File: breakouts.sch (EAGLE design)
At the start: 7 parts

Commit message: Added USB C breakout with CC pulldown resistors
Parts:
- added CONN2: USB-C_WURTH_632723X00011USB-C, USB-C:USB-C_WURTH_632723X00011USB-C
- added JP1: (no value), SparkFun:M06SIP
- added R2, R3: 5K1, SparkFun-Passives:RESISTOR0603-RES
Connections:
- removed net N$10: U$2.NC
- new net CC1_SA: CONN2.CC1, JP1.2, R3.2
- new net CC2_SA: CONN2.CC2, JP1.3, R2.2
- new net DN_SA: CONN2.DN1, CONN2.DN2, JP1.5
- new net DP_SA: CONN2.DP1, CONN2.DP2, JP1.4
- new net VBUS_SA: CONN2.VBUS1, CONN2.VBUS2, CONN2.VBUS3, CONN2.VBUS4, JP1.1
- net GND: now also CONN1.SHIELD5, CONN1.SHIELD6, CONN1.SHIELD7, CONN1.SHIELD8, CONN2.GND0, CONN2.GND1, CONN2.GND3, CONN2.GND4, CONN2.SHIELD1, CONN2.SHIELD2, CONN2.SHIELD3, CONN2.SHIELD4, CONN2.SHIELD5, CONN2.SHIELD6, CONN2.SHIELD7, CONN2.SHIELD8, JP1.6, R2.1, R3.1
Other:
- note added: "USBC breakout"
- note added: "optional pulldown resistors for UFP operation"

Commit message: Added RJ12 breakout
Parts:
- added J1: RJ11, SparkFun-Connectors:RJ11-6PTH
- added JP2: (no value), SparkFun:M06SIP
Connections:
- new net N$1: J1.1, JP2.1
- new net N$2: J1.2, JP2.2
- new net N$3: J1.3, JP2.3
- new net N$4: J1.4, JP2.4
- new net N$5: J1.5, JP2.5
- new net N$6: J1.6, JP2.6
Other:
- note added: "RJ12 breakout"
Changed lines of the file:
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@@
 <layer number="54" name="bGND_GNDA" color="1" fill="9" visible="yes" active="no"/>
 <layer number="56" name="wert" color="7" fill="1" visible="yes" active="no"/>
+<layer number="57" name="tCAD" color="7" fill="1" visible="no" active="no"/>
+<layer number="90" name="Modules" color="5" fill="1" visible="yes" active="yes"/>
 <layer number="91" name="Nets" color="2" fill="1" visible="yes" active="yes"/>
 <layer number="92" name="Busses" color="1" fill="1" visible="yes" active="yes"/>
@@
 <layer number="97" name="Info" color="7" fill="1" visible="yes" active="yes"/>
 <layer number="98" name="Guide" color="6" fill="1" visible="yes" active="yes"/>
+<layer number="99" name="SpiceOrder" color="7" fill="1" visible="yes" active="yes"/>
 <layer number="100" name="Muster" color="7" fill="1" visible="no" active="no"/>
 <layer number="101" name="Patch_Top" color="12" fill="4" visible="yes" active="yes"/>
@@
 <layer number="108" name="tplace-old" color="10" fill="1" visible="yes" active="yes"/>
 <layer number="109" name="ref-old" color="11" fill="1" visible="yes" active="yes"/>
+<layer number="110" name="fp0" color="7" fill="1" visible="yes" active="yes"/>
+<layer number="111" name="LPC17xx" color="7" fill="1" visible="yes" active="yes"/>
+<layer number="112" name="tSilk" color="7" fill="1" visible="yes" active="yes"/>
+<layer number="113" name="IDFDebug" color="4" fill="1" visible="yes" active="yes"/>
 <layer number="116" name="Patch_BOT" color="9" fill="4" visible="yes" active="yes"/>
 <layer number="121" name="_tsilk" color="7" fill="1" visible="yes" active="yes"/>
 <layer number="122" name="_bsilk" color="7" fill="1" visible="yes" active="yes"/>
+<layer number="123" name="tTestmark" color="7" fill="1" visible="yes" active="yes"/>
+<layer number="124" name="bTestmark" color="7" fill="1" visible="yes" active="yes"/>
 <layer number="125" name="_tNames" color="7" fill="1" visible="yes" active="yes"/>
+<layer number="126" name="_bNames" color="7" fill="1" visible="yes" active="yes"/>
+<layer number="127" name="_tValues" color="7" fill="1" visible="yes" active="yes"/>
+<layer number="128" name="_bValues" color="7" fill="1" visible="yes" active="yes"/>
+<layer number="131" name="tAdjust" color="7" fill="1" visible="yes" active="yes"/>
+<layer number="132" name="bAdjust" color="7" fill="1" visible="yes" active="yes"/>
 <layer number="144" name="Drill_legend" color="7" fill="1" visible="yes" active="yes"/>
+<layer number="150" name="Notes" color="7" fill="1" visible="yes" active="yes"/>
 <layer number="151" name="HeatSink" color="7" fill="1" visible="yes" active="yes"/>
+<layer number="152" name="_bDocu" color="7" fill="1" visible="yes" active="yes"/>
+<layer number="153" name="FabDoc1" color="7" fill="1" visible="yes" active="yes"/>
+<layer number="154" name="FabDoc2" color="7" fill="1" visible="yes" active="yes"/>
+<layer number="155" name="FabDoc3" color="7" fill="1" visible="yes" active="yes"/>
 <layer number="199" name="Contour" color="7" fill="1" visible="yes" active="yes"/>
 <layer number="200" name="200bmp" color="1" fill="10" visible="yes" active="yes"/>
@@
 <layer number="223" name="223bmp" color="24" fill="1" visible="no" active="no"/>
 <layer number="224" name="224bmp" color="25" fill="1" visible="no" active="no"/>
+<layer number="248" name="Housing" color="7" fill="1" visible="yes" active="yes"/>
+<layer number="249" name="Edge" color="7" fill="1" visible="yes" active="yes"/>
 <layer number="250" name="Descript" color="3" fill="1" visible="no" active="no"/>
 <layer number="251" name="SMDround" color="12" fill="11" visible="no" active="no"/>
@@
 <part name="R3" library="SparkFun-Passives" deviceset="RESISTOR" device="0603-RES" value="5K1"/>
 <part name="JP1" library="SparkFun" deviceset="M06" device="SIP"/>
+<part name="J1" library="SparkFun-Connectors" deviceset="RJ11-6" device="PTH" value="RJ11"/>
+<part name="JP2" library="SparkFun" deviceset="M06" device="SIP"/>
 </parts>
 <sheets>
@@
 <wire x1="-266.7" y1="-78.74" x2="-266.7" y2="129.54" width="1.6764" layer="97"/>
 <text x="-175.26" y="17.78" size="6.4516" layer="97">USBC breakout</text>
+<text x="-220.98" y="-121.92" size="6.4516" layer="97">RJ12 breakout</text>
+<wire x1="-157.48" y1="-152.4" x2="-228.6" y2="-152.4" width="1.6764" layer="97"/>
+<wire x1="-157.48" y1="-152.4" x2="-157.48" y2="-101.6" width="1.6764" layer="97"/>
+<wire x1="-157.48" y1="-101.6" x2="-228.6" y2="-101.6" width="1.6764" layer="97"/>
+<wire x1="-228.6" y1="-101.6" x2="-228.6" y2="-152.4" width="1.6764" layer="97"/>
 </plain>
 <instances>
@@
 <instance part="R3" gate="G$1" x="-149.86" y="71.12" rot="R90"/>
 <instance part="JP1" gate="G$1" x="-114.3" y="71.12" rot="R180"/>
+<instance part="J1" gate="G$1" x="-210.82" y="-137.16"/>
+<instance part="JP2" gate="G$1" x="-187.96" y="-137.16"/>
 </instances>
 <busses>
@@
 </segment>
 </net>
+<net name="N$1" class="0">
+<segment>
+<pinref part="J1" gate="G$1" pin="1"/>
+<pinref part="JP2" gate="G$1" pin="1"/>
+<wire x1="-205.74" y1="-142.24" x2="-182.88" y2="-142.24" width="0.1524" layer="91"/>
+</segment>
+</net>
+<net name="N$2" class="0">
+<segment>
+<pinref part="JP2" gate="G$1" pin="2"/>
+<pinref part="J1" gate="G$1" pin="2"/>
+<wire x1="-182.88" y1="-139.7" x2="-205.74" y2="-139.7" width="0.1524" layer="91"/>
+</segment>
+</net>
+<net name="N$3" class="0">
+<segment>
+<pinref part="J1" gate="G$1" pin="3"/>
+<pinref part="JP2" gate="G$1" pin="3"/>
+<wire x1="-205.74" y1="-137.16" x2="-182.88" y2="-137.16" width="0.1524" layer="91"/>
+</segment>
+</net>
+<net name="N$4" class="0">
+<segment>
+<pinref part="JP2" gate="G$1" pin="4"/>
+<pinref part="J1" gate="G$1" pin="4"/>
+<wire x1="-182.88" y1="-134.62" x2="-205.74" y2="-134.62" width="0.1524" layer="91"/>
+</segment>
+</net>
+<net name="N$5" class="0">
+<segment>
+<pinref part="J1" gate="G$1" pin="5"/>
+<pinref part="JP2" gate="G$1" pin="5"/>
+<wire x1="-205.74" y1="-132.08" x2="-182.88" y2="-132.08" width="0.1524" layer="91"/>
+</segment>
+</net>
+<net name="N$6" class="0">
+<segment>
+<pinref part="JP2" gate="G$1" pin="6"/>
+<pinref part="J1" gate="G$1" pin="6"/>
+<wire x1="-182.88" y1="-129.54" x2="-205.74" y2="-129.54" width="0.1524" layer="91"/>
+</segment>
+</net>

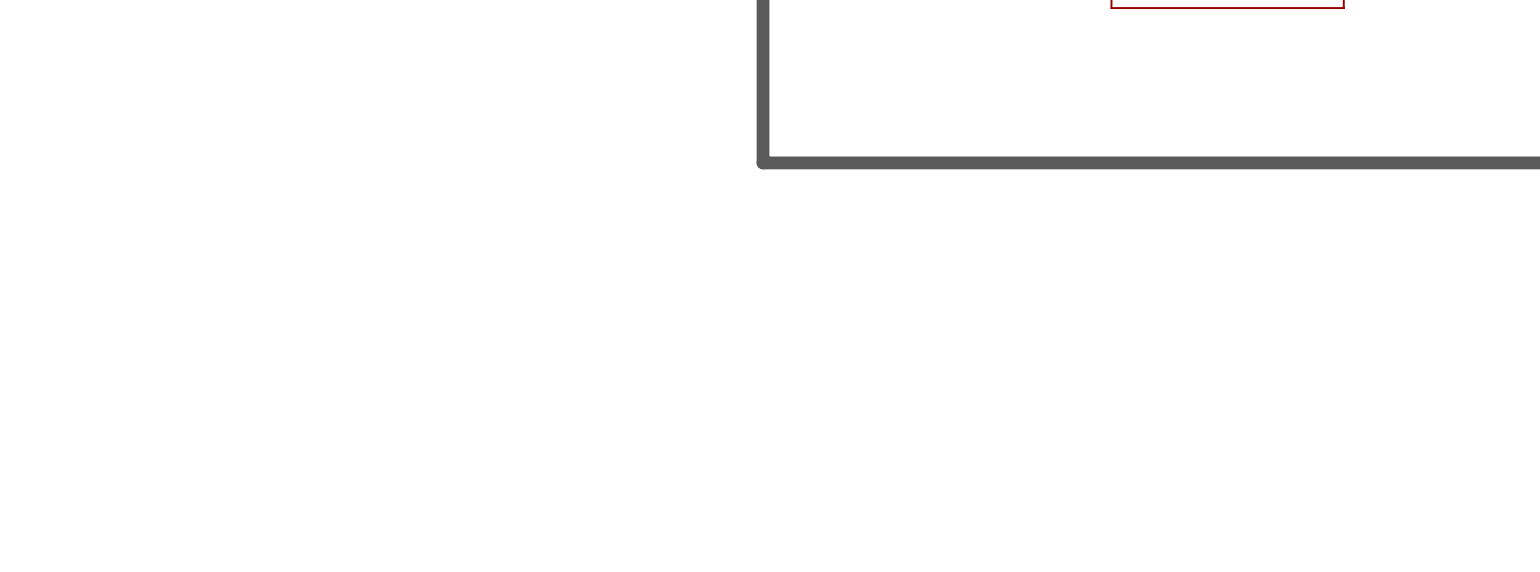
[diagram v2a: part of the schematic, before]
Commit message: Panalised breakouts and added powerpole breakout
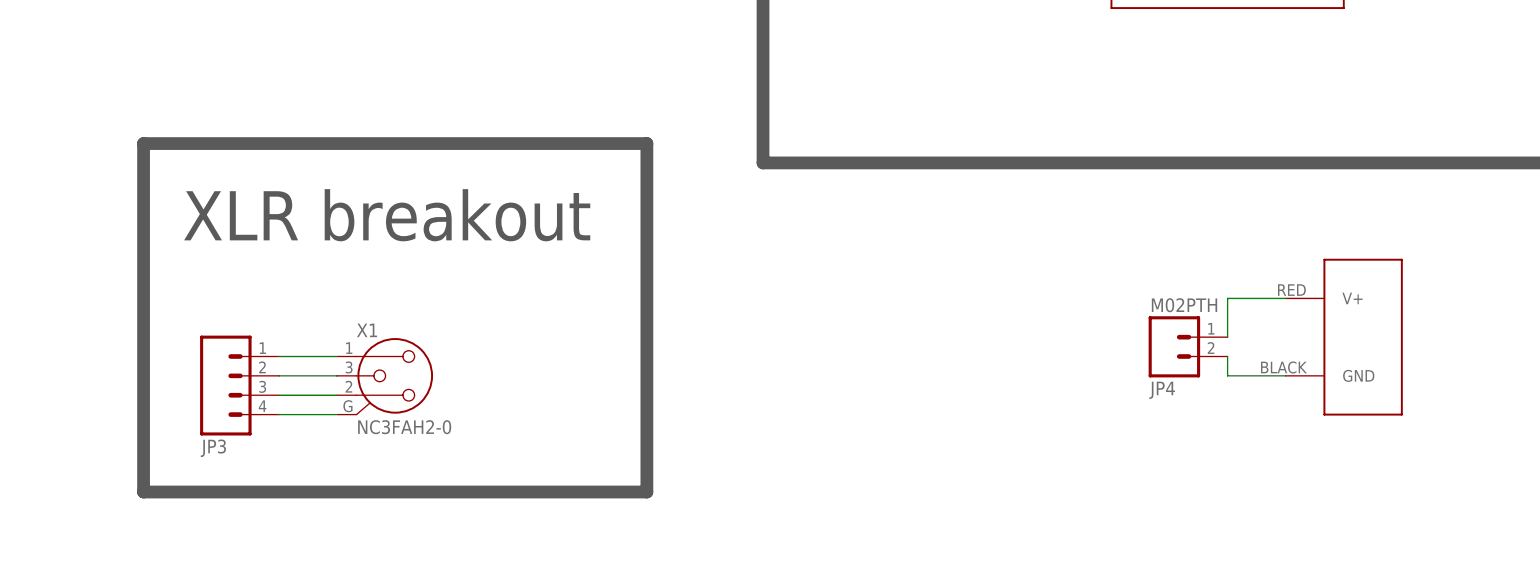
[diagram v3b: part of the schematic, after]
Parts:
- added J2: POWERPOLE_POWER25A, powerpoles:POWERPOLE_POWER25A
- added JP3: (no value), SparkFun-Connectors:M04PTH
- added JP4: M02PTH, SparkFun-Connectors:M02PTH
- added X1: NC3FAH2-0, con-neutrik_ag:NC3FAH2-0
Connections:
- new net N$10: JP3.3, X1.2
- new net N$11: JP3.4, X1.G
- new net N$12: J2.V+, JP4.1
- new net N$13: J2.GND, JP4.2
- new net N$7: JP3.1, X1.1
- new net N$8: JP3.2, X1.3
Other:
- note added: "XLR breakout"
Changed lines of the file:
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@@
 <part name="J1" library="SparkFun-Connectors" deviceset="RJ11-6" device="PTH" value="RJ11"/>
 <part name="JP2" library="SparkFun" deviceset="M06" device="SIP"/>
+<part name="X1" library="con-neutrik_ag" deviceset="NC3" device="FAH2-0"/>
+<part name="JP3" library="SparkFun-Connectors" deviceset="M04" device="PTH"/>
+<part name="J2" library="powerpoles" deviceset="POWERPOLE_POWER" device="25A"/>
+<part name="JP4" library="SparkFun-Connectors" deviceset="M02" device="PTH"/>
 </parts>
 <sheets>
@@
 <wire x1="-157.48" y1="-101.6" x2="-228.6" y2="-101.6" width="1.6764" layer="97"/>
 <wire x1="-228.6" y1="-101.6" x2="-228.6" y2="-152.4" width="1.6764" layer="97"/>
+<wire x1="-111.76" y1="-99.06" x2="-45.72" y2="-99.06" width="1.6764" layer="97"/>
+<wire x1="-45.72" y1="-99.06" x2="-45.72" y2="-144.78" width="1.6764" layer="97"/>
+<wire x1="-45.72" y1="-144.78" x2="-111.76" y2="-144.78" width="1.6764" layer="97"/>
+<wire x1="-111.76" y1="-144.78" x2="-111.76" y2="-99.06" width="1.6764" layer="97"/>
+<text x="-106.68" y="-111.76" size="6.4516" layer="97">XLR breakout</text>
 </plain>
 <instances>
@@
 <instance part="J1" gate="G$1" x="-210.82" y="-137.16"/>
 <instance part="JP2" gate="G$1" x="-187.96" y="-137.16"/>
+<instance part="X1" gate="G$1" x="-78.74" y="-129.54"/>
+<instance part="JP3" gate="G$1" x="-99.06" y="-129.54" rot="MR180"/>
+<instance part="J2" gate="G$1" x="48.26" y="-124.46"/>
+<instance part="JP4" gate="G$1" x="22.86" y="-124.46" rot="MR180"/>
 </instances>
 <busses>
@@
 </segment>
 </net>
+<net name="N$7" class="0">
+<segment>
+<pinref part="JP3" gate="G$1" pin="1"/>
+<pinref part="X1" gate="G$1" pin="1"/>
+<wire x1="-93.98" y1="-127" x2="-86.36" y2="-127" width="0.1524" layer="91"/>
+</segment>
+</net>
+<net name="N$8" class="0">
+<segment>
+<pinref part="X1" gate="G$1" pin="3"/>
+<pinref part="JP3" gate="G$1" pin="2"/>
+<wire x1="-86.36" y1="-129.54" x2="-93.98" y2="-129.54" width="0.1524" layer="91"/>
+</segment>
+</net>
+<net name="N$10" class="0">
+<segment>
+<pinref part="JP3" gate="G$1" pin="3"/>
+<pinref part="X1" gate="G$1" pin="2"/>
+<wire x1="-93.98" y1="-132.08" x2="-86.36" y2="-132.08" width="0.1524" layer="91"/>
+</segment>
+</net>
+<net name="N$11" class="0">
+<segment>
+<pinref part="X1" gate="G$1" pin="G"/>
+<pinref part="JP3" gate="G$1" pin="4"/>
+<wire x1="-86.36" y1="-134.62" x2="-93.98" y2="-134.62" width="0.1524" layer="91"/>
+</segment>
+</net>
+<net name="N$12" class="0">
+<segment>
+<pinref part="J2" gate="G$1" pin="V+"/>
+<pinref part="JP4" gate="G$1" pin="1"/>
+<wire x1="38.1" y1="-119.38" x2="30.48" y2="-119.38" width="0.1524" layer="91"/>
+<wire x1="30.48" y1="-119.38" x2="30.48" y2="-124.46" width="0.1524" layer="91"/>
+</segment>
+</net>
+<net name="N$13" class="0">
+<segment>
+<pinref part="J2" gate="G$1" pin="GND"/>
+<pinref part="JP4" gate="G$1" pin="2"/>
+<wire x1="38.1" y1="-129.54" x2="30.48" y2="-129.54" width="0.1524" layer="91"/>
+<wire x1="30.48" y1="-129.54" x2="30.48" y2="-127" width="0.1524" layer="91"/>
+</segment>
+</net>
